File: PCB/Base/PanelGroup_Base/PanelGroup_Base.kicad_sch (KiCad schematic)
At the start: 64 parts, among them J1 J_DIAG, J11 J_BREAKOUT, J2 J_BL1, J3 J_I2C2, J4 J_I2C1, J5 J_CAN_TERM, J6 J_BL2, J7 J_SWD, J8 J_BUS_IN, J9 J_BUS_OUT, Q2 AO3400A, Q3 AO3400A, SW1 RESET, U1 STM32F103C8Tx, U2 SN65HVD230, U3 AMS1117-3.3, Y1 8MHz

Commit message: refactor(pcb): genericize backlight FET symbol (IRLML2502 -> Q_NMOS_GSD)
The custom symbol was part-named IRLML2502, but the fitted part is the
AO3400A (30V, per the #232 backlight-FET standard) applied via a
per-instance Value/IPN override. Rename the shared symbol to a generic
N-FET donor so the name no longer implies a specific part: identity lives
in the instance Value + IPN (IPN convention), the symbol is just the
SOT-23 GSD footprint/pinout.

- OpenSkyhawk.kicad_sym: symbol IRLML2502 -> Q_NMOS_GSD; scrub the
  IRLML2502-specific Value/Description/Datasheet (was "20V ... Vgsth
  0.3-0.7V" + Infineon link) to a generic SOT-23 N-FET description.
- PanelGroup_Base + ASN-41_NavComputer: retarget the two FET instances'
  lib_id. Instance Value stays AO3400A; footprint (SOT-23) and pins
  (1/2/3 GSD) unchanged -> no reroute.
- Armament_MCU left on IRLML2502 (board being retired).

ERC clean on both live boards (kicad-cli sch erc, 0 violations).
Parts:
- Q2, Q3: symbol OpenSkyhawk:IRLML2502 -> OpenSkyhawk:Q_NMOS_GSD
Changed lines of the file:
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@@
 	)
 	(symbol
-		(lib_id "OpenSkyhawk:IRLML2502")
+		(lib_id "OpenSkyhawk:Q_NMOS_GSD")
 		(at 191.77 106.68 0)
 		(unit 1)
@@
 	)
 	(symbol
-		(lib_id "OpenSkyhawk:IRLML2502")
+		(lib_id "OpenSkyhawk:Q_NMOS_GSD")
 		(at 213.36 135.89 0)
 		(unit 1)

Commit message: feat(pcb): +12V bulk cap → 22µF/35V electrolytic reroute (#236) (#243)
## What
Replaces the **+12V bulk cap** across ASN-41, PDU, Gateway_Bridge and
PanelGroup_Base:
**10µF/35V ceramic (0805) → 22µF/35V aluminium electrolytic**
`C48971029` (`Capacitor_SMD:CP_Elec_5x5.4`).

## Why (#236)
- 10µF/35V *ceramic* on a 12V rail DC-bias-derates to ~4–6µF;
electrolytic holds full value at ~1/5 the cost.
- Footprint grows 0805 → Ø5 (35V elec), so fabbed boards get a reroute;
value taken to 22µF (same Ø5 can) for margin.

## Changes
- Symbol fields updated: IPN `CAP-ELEC-22UF-35V-D5`, LCSC `C48971029`,
Rating `35V`, Tolerance `20%`.
- **PDU (C9), Gateway_Bridge (C15), PanelGroup_Base (C15)** — rerouted
for the Ø5 land; board revision **0.1.0 → 0.2.0**.
- **ASN-41 (C15)** — unrouted, schematic only; revision **0.1.0**.

## Verification
- ERC clean (0/0) on all four boards.
- CI (KiCad PR Reports) runs ERC/DRC.

Closes #236 — the +12V ceramic→electrolytic reroute was the
consolidation's last open action; the rest is decided and applied (per
#235 + this PR).
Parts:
- removed C15: 10uF, Capacitor_SMD:C_0805_2012Metric, symbol Device:C
- added C15: 22uF, Capacitor_SMD:CP_Elec_5x5.4, symbol Device:C_Polarized_Small
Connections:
- net +12V: now also C15.1
- net GND: now also C15.2

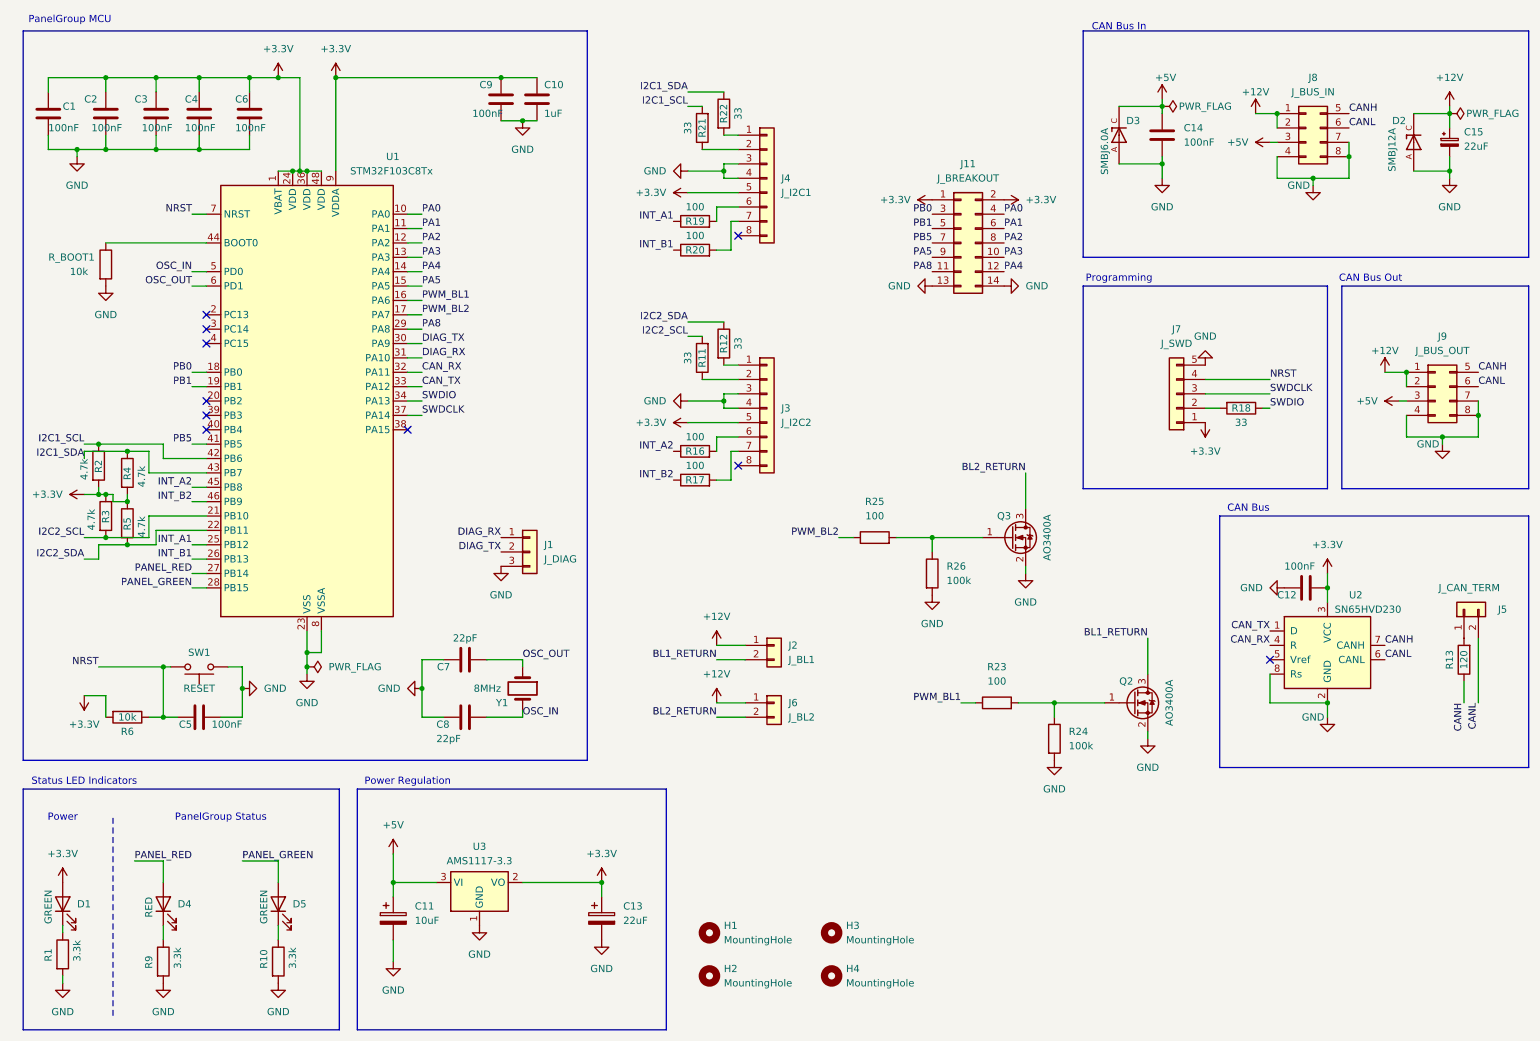
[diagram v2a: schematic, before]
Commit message: feat(pcb): base boards Rev 2 — PanelGroup ShiftBus remap + Gateway/PDU fab prep (#209) (#302)
Takes PanelGroup base to Rev 2 for the 74HC ShiftBus pin standard, and
prepares
Gateway_Bridge and PDU for the same fab run. Boards are ordered — JLC
`W2026093021050394`, LCSC `WM2610010130` — so this is the as-fabricated
state.

## PanelGroup base Rev 2 (#209)

- **`J_SR` ShiftBus connector** (XH-7): `SCK · MOSI · MISO · GND · 3.3V
· LOAD · LTCH`,
  with 33 Ω series termination at the driver on SCK / LOAD / LATCH.
- **Nine-pin re-map.** I²C2 interrupts move PB8/PB9 → PA8/PA15 to free
the ShiftBus
strobes; J11 positions 7 and 11 become PB2 and PC14. PB2/PC14 are chosen
so the
breakout never collides with the I²C interrupt EXTI lines, which are
shared by pin
  number across ports.
- Docs rewritten from the final netlist: `docs/_source/base-boards.md`,
plus the
  INT-pin guidance and the now-adopted `J_SR` standard.

All four Rev 1 pre-order bench checks passed, so no finding forced a Rev
2 change —
CAN at 502 kbps with ACK from a second node, I²C pull-ups and both buses
end to end,
backlight PWM at 1.000 kHz with the gate pull-downs holding through
reset. Results are
recorded in #209.

## Gateway_Bridge and PDU — fab prep

Both boards had diverged from their fabbed revision (#243 moved the +12
V bulk cap to a
22 µF/35 V electrolytic, and Gateway gained the input-rail TVS with **no
pads on the old
board**), and neither had been assembled — so both were re-fabbed rather
than built as-is.

The silkscreen gate caught three real defects on Gateway before fab:

- revision text still read `0.1.0`
- **J8/J9 (`J_BUS_IN`/`J_BUS_OUT`) had no pin labels at all** — 12 V and
CAN on two
  identical unkeyed Mini-Fit connectors side by side
- **J1 (`J_DIAG`, the serial console) was labelled `SDA`/`SCL`** instead
of `RX`/`TX`

Also fixed a `CAN TERM` legend implemented by overriding the footprint
`Value` field,
which raised a parity error and would have been silently erased by the
next schema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
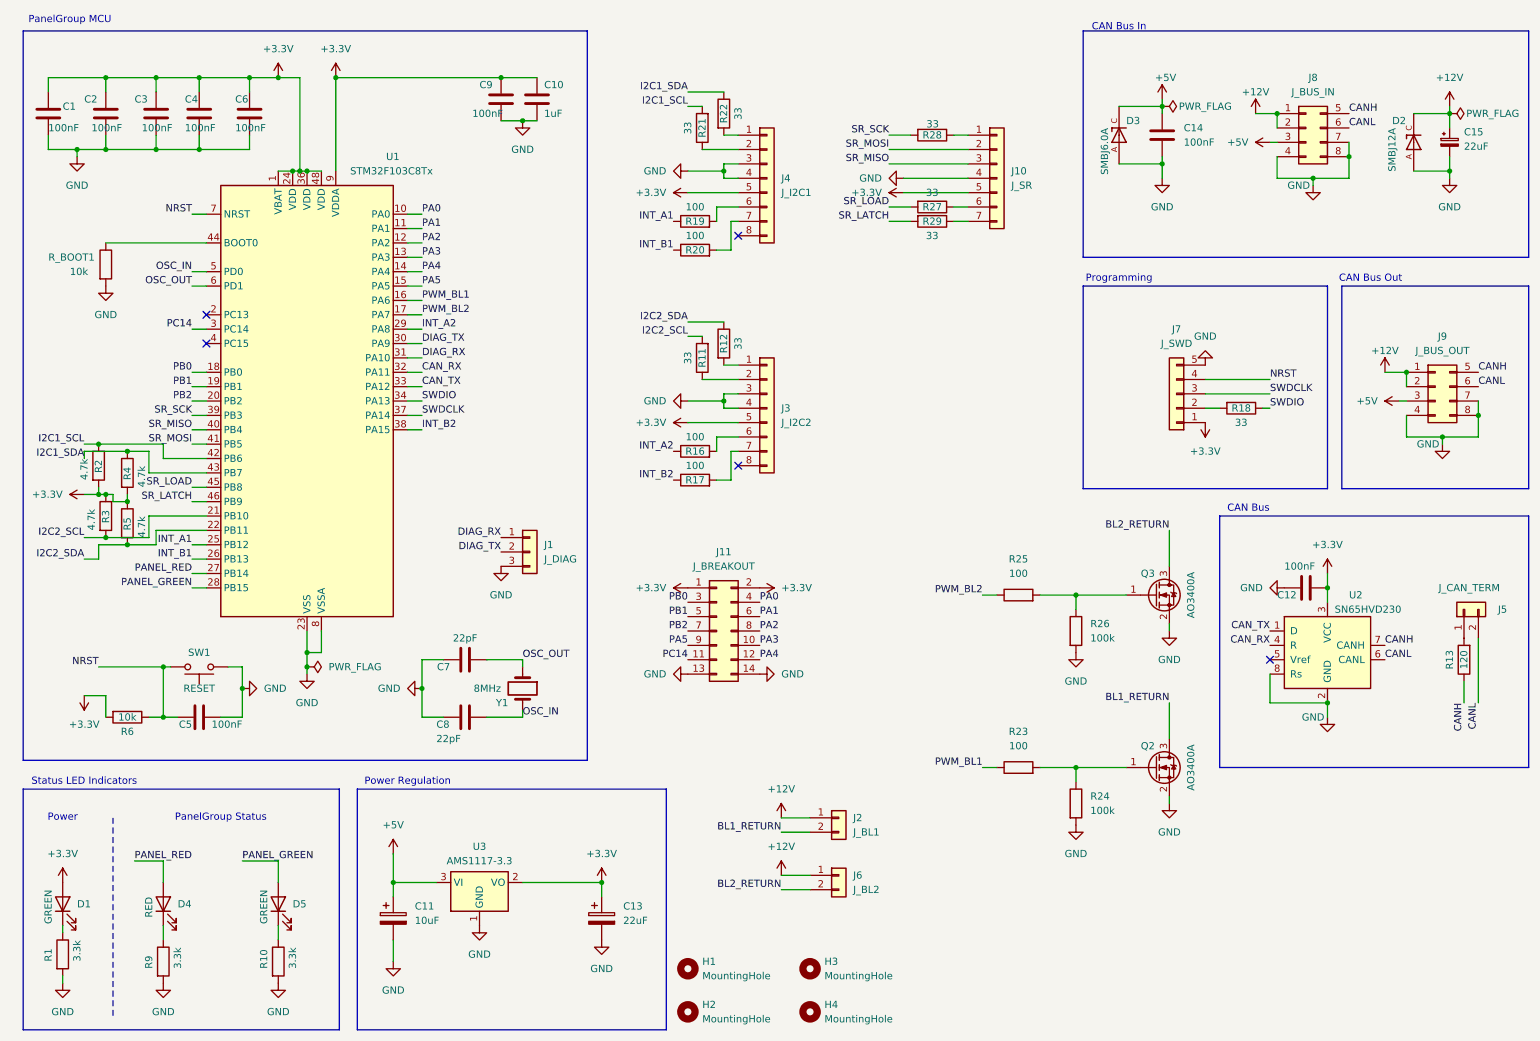
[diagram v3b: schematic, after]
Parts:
- added J10: J_SR, Connector_JST:JST_XH_B7B-XH-A_1x07_P2.50mm_Vertical, symbol Connector_Generic:Conn_01x07
- added R27, R28, R29: 33, Resistor_SMD:R_0805_2012Metric, symbol Device:R
- J11: IPN CONN-HDR-2P -> CONN-HDR-2X7P
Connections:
- net +3.3V: now also J10.5 (Pin_5)
- net GND: now also J10.4 (Pin_4)
- net INT_A2: now also U1.29 (PA8); no longer U1.45 (PB8)
- net INT_B2: now also U1.38 (PA15); no longer U1.46 (PB9)
- net PB2: now reaches U1.20 (PB2)
- net PB2: now also J11.7 (Pin_7)
- net PC14: now reaches U1.3 (PC14)
- net PC14: now also J11.11 (Pin_11)
- net SR_SCK: now reaches U1.39 (PB3)
- net SR_SCK: now also R28.2
- net SR_MISO: now reaches U1.40 (PB4)
- net SR_MISO: now also J10.3 (Pin_3)
- removed net PA8: J11.11 (Pin_11), U1.29 (PA8)
- net PB5 renamed SR_MOSI
- net SR_MOSI: now also J10.2 (Pin_2); no longer J11.7 (Pin_7)
- new net: J10.6 (Pin_6), R27.1
- new net: J10.7 (Pin_7), R29.1
- new net: J10.1 (Pin_1), R28.1
- new net SR_LATCH: R29.2, U1.46 (PB9)
- new net SR_LOAD: R27.2, U1.45 (PB8)
- no-connect marks 10 -> 5
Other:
- moved on the sheet: H1, H2, H3, H4, J11, J2, J6, Q2, Q3, R23, R24, R25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
